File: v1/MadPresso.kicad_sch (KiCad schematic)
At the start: 38 parts, among them J1 Conn_01x07, J2 Conn_01x03, Q1 2N7002, Q2 2N7002, Q3 BC847, U1 LTV-356T, U2 WeMos_D1_mini

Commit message: final touches for v1
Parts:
- J2: footprint Connector_PinHeader_2.54mm:PinHeader_1x03_P2.54mm_Horizontal -> Connector_JST:JST_PH_S3B-PH-K_1x03_P2.00mm_Horizontal
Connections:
- net +5V: now also J2.1 (Pin_1); no longer J2.3 (Pin_3)
- net at R9.2: now also J2.3 (Pin_3); no longer J2.1 (Pin_1)
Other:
- moved on the sheet: J2
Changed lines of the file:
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@@
   (junction (at 262.636 31.75) (diameter 1.016) (color 0 0 0 0))
   (junction (at 262.636 41.91) (diameter 1.016) (color 0 0 0 0))
+  (no_connect (at 252.095 86.995))
   (no_connect (at 231.775 86.995))
+  (no_connect (at 231.775 76.835))
   (no_connect (at 231.775 84.455))
-  (no_connect (at 231.775 76.835))
-  (no_connect (at 252.095 86.995))
   (wire (pts (xy 21.59 169.672) (xy 29.845 169.672))
     (stroke (width 0) (type solid) (color 0 0 0 0))
@@
     )
   )
-  (symbol (lib_id "Connector_Generic:Conn_01x03") (at 64.77 38.735 180) (unit 1)
-    (in_bom yes) (on_board yes)
-    (property "Reference" "J2" (id 0) (at 66.802 30.6132 0))
-    (property "Value" "Conn_01x03" (id 1) (at 66.802 32.9119 0))
-    (property "Footprint" "Connector_PinHeader_2.54mm:PinHeader_1x03_P2.54mm_Horizontal" (id 2) (at 64.77 38.735 0)
+  (symbol (lib_id "Connector_Generic:Conn_01x03") (at 64.77 38.735 0) (mirror y) (unit 1)
+    (in_bom yes) (on_board yes)
+    (property "Reference" "J2" (id 0) (at 64.643 30.3468 0))
+    (property "Value" "Conn_01x03" (id 1) (at 64.77 32.8741 0))
+    (property "Footprint" "Connector_JST:JST_PH_S3B-PH-K_1x03_P2.00mm_Horizontal" (id 2) (at 64.77 38.735 0)
       (effects (font (size 1.27 1.27)) hide)
     )
@@
     )
     (path "/3b67d7d9-14f9-46f2-9c26-7ea51b8e981b"
-      (reference "J2") (unit 1) (value "Conn_01x03") (footprint "Connector_PinHeader_2.54mm:PinHeader_1x03_P2.54mm_Horizontal")
+      (reference "J2") (unit 1) (value "Conn_01x03") (footprint "Connector_JST:JST_PH_S3B-PH-K_1x03_P2.00mm_Horizontal")
     )
     (path "/d88f3030-1974-43e3-8892-faa2a80ca689"

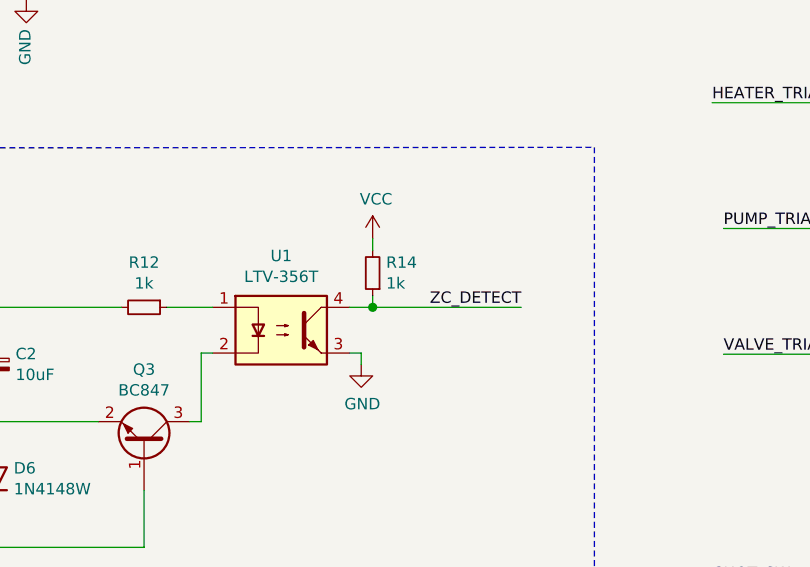
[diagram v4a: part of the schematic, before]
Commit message: Value change for v1
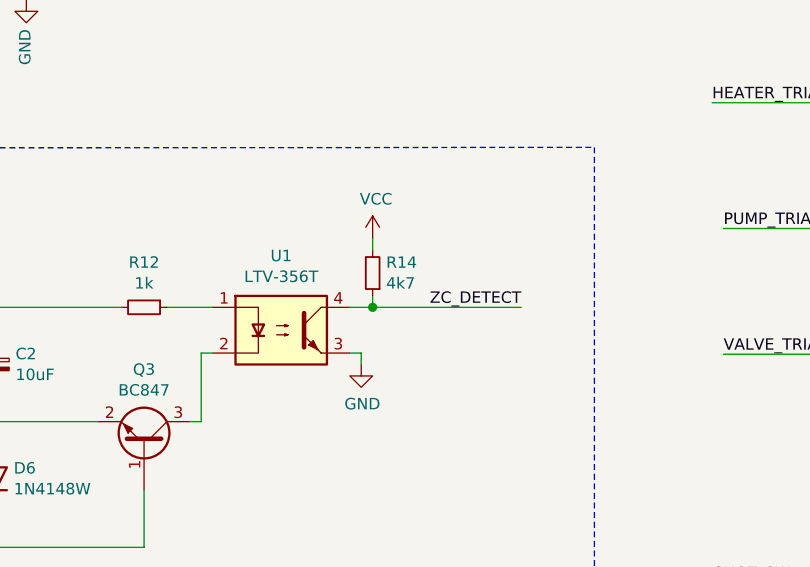
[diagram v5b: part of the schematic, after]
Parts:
- R14: value 1k -> 4k7
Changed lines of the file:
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@@
       (effects (font (size 1.27 1.27)) (justify right))
     )
-    (property "Value" "1k" (id 1) (at 116.8146 86.741 0)
+    (property "Value" "4k7" (id 1) (at 116.8146 86.741 0)
       (effects (font (size 1.27 1.27)) (justify right))
     )
@@
     )
     (path "/00000000-0000-0000-0000-00005ffe1cf2"
-      (reference "R14") (unit 1) (value "1k") (footprint "Resistor_SMD:R_0603_1608Metric_Pad1.05x0.95mm_HandSolder")
+      (reference "R14") (unit 1) (value "4k7") (footprint "Resistor_SMD:R_0603_1608Metric_Pad1.05x0.95mm_HandSolder")
     )
     (path "/00000000-0000-0000-0000-0000604d5951"
